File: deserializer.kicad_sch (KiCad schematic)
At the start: 49 parts, among them U7 MAX96724GTN_VY+, Y1 Resonator_25MHz_ABM8G

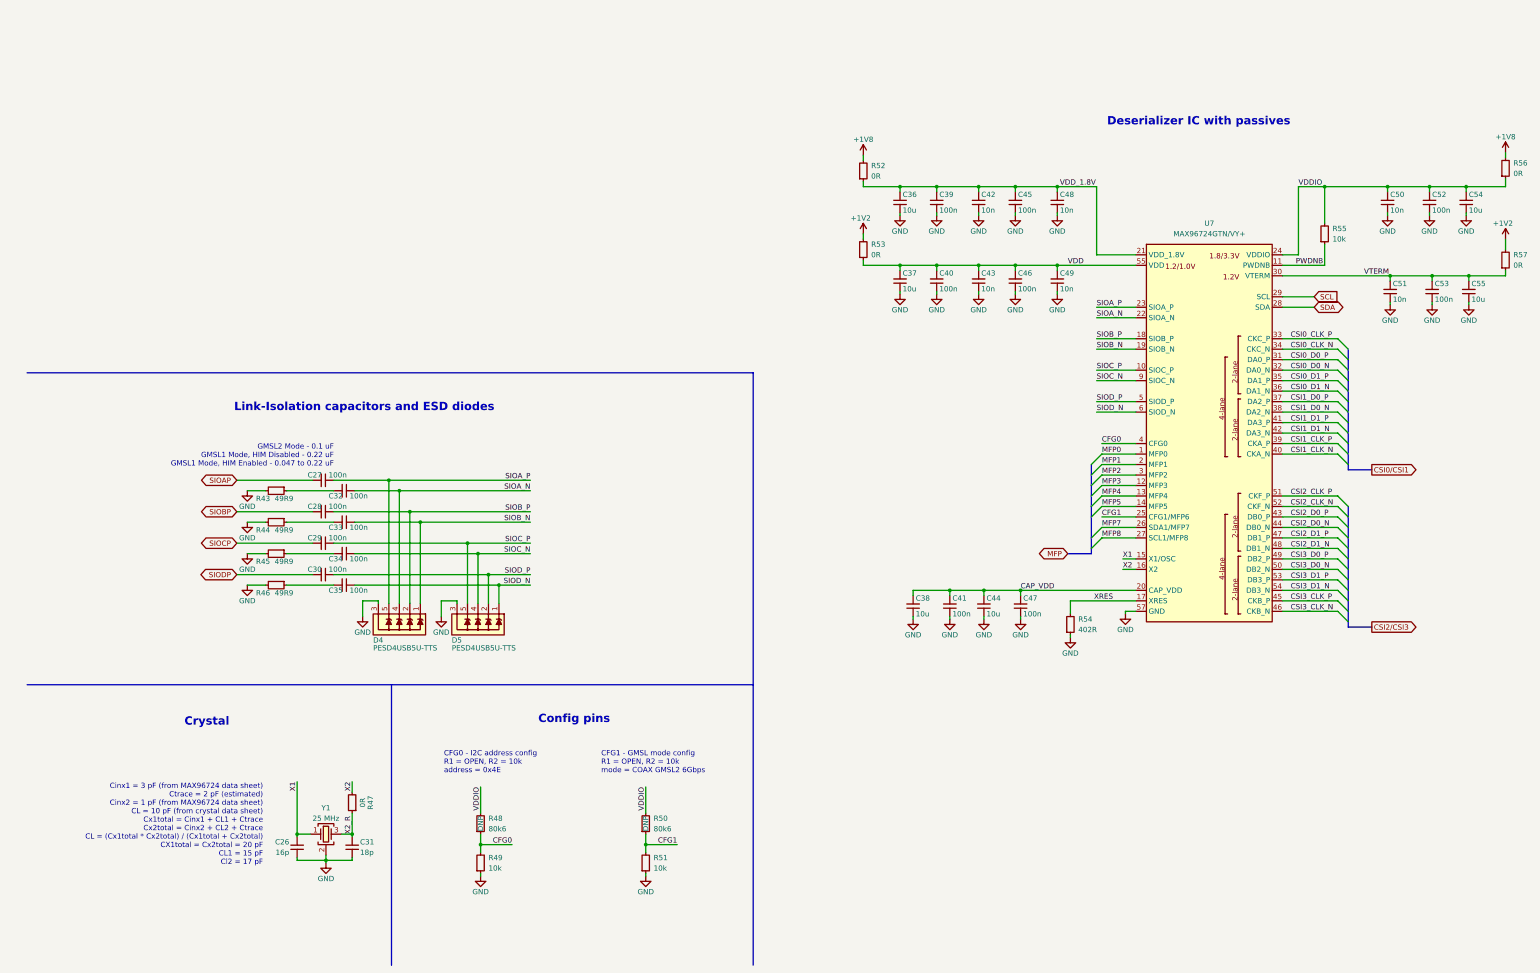
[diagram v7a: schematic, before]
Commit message: Schematics: Fix buses, change labels to hierarchical
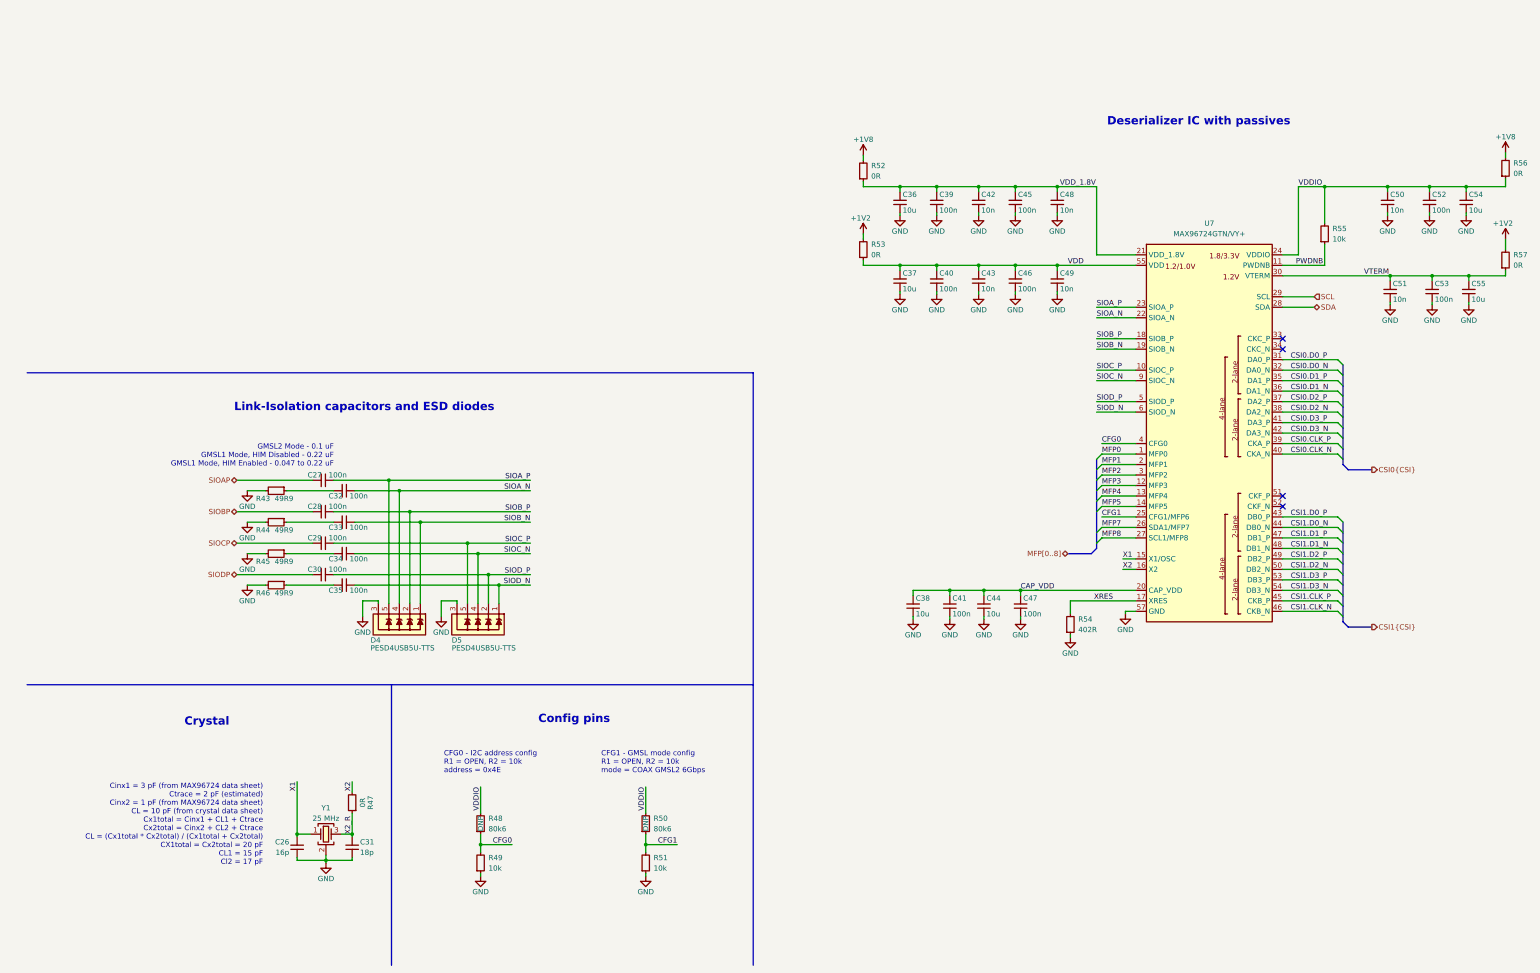
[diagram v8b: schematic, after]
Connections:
- net CSI0_CLK_N: no longer names the net of U7.34 (CKC_N)
- net CSI0_CLK_P: no longer names the net of U7.33 (CKC_P)
- net CSI0_D0_N renamed CSI0.D0_N
- net CSI0_D0_P renamed CSI0.D0_P
- net CSI0_D1_N renamed CSI0.D1_N
- net CSI0_D1_P renamed CSI0.D1_P
- net CSI1_CLK_N renamed CSI0.CLK_N
- net CSI1_CLK_P renamed CSI0.CLK_P
- net CSI1_D0_N renamed CSI0.D2_N
- net CSI1_D0_P renamed CSI0.D2_P
- net CSI1_D1_N renamed CSI0.D3_N
- net CSI1_D1_P renamed CSI0.D3_P
- net CSI2_CLK_N: no longer names the net of U7.52 (CKF_N)
- net CSI2_CLK_P: no longer names the net of U7.51 (CKF_P)
- net CSI2_D0_N renamed CSI1.D0_N
- net CSI2_D0_P renamed CSI1.D0_P
- net CSI2_D1_N renamed CSI1.D1_N
- net CSI2_D1_P renamed CSI1.D1_P
- net CSI3_CLK_N renamed CSI1.CLK_N
- net CSI3_CLK_P renamed CSI1.CLK_P
- net CSI3_D0_N renamed CSI1.D2_N
- net CSI3_D0_P renamed CSI1.D2_P
- net CSI3_D1_N renamed CSI1.D3_N
- net CSI3_D1_P renamed CSI1.D3_P
- new net: D4.10, D4.6, D4.7, D4.9
- new net: D5.10, D5.6, D5.7, D5.9
- no-connect marks 0 -> 4
